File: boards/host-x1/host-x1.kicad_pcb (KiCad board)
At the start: 4 copper layers, 91 x 83 mm, 231 parts, among them J1 CONN_3_PWROUT, J2 XILINX_JTAG, J3 STARSHIPRAIDER_IOBOARD_HOST, J4 BEL_FUSE_0826-1G1T-23-F, J5 PMOD_HEADER, M1 LOGO_LONGTHING, M2 LOGO_ROHS, M3 LOGO_WEEE, M4 HOLE, M5 HOLE, M6 HOLE, M7 HOLE, Q1 SSM6N58NU, Q2 SSM6N58NU, Q3 SSM6N58NU, Q4 SSM6N58NU, SW1 SW_Push, U1 OLK-T_3-W12P-C, U10 DSC6102CI2A-100.0000, U11 S25FS064S_BGA, U2 XC7A100T-1FTG256C, U3 LTC3374-QFN, U4 S27KS0641DPBHI02, U5 S27KS0641DPBHI02, U6 S27KS0641DPBHI02, U7 S27KS0641DPBHI02, U8 KSZ9031RN, U9 DSC6101CI2A-025.0000

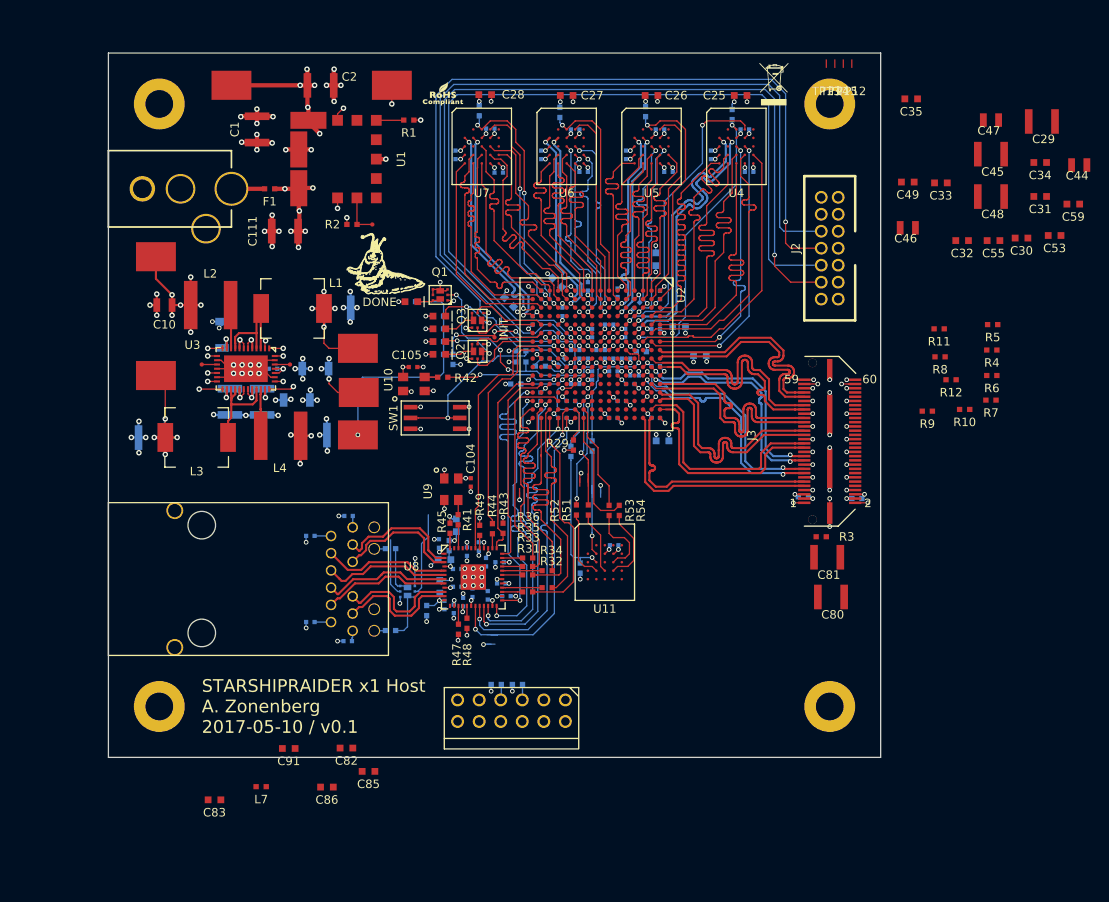
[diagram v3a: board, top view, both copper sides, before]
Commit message: Miscellaneous detail routing. Added some PMOD header connections
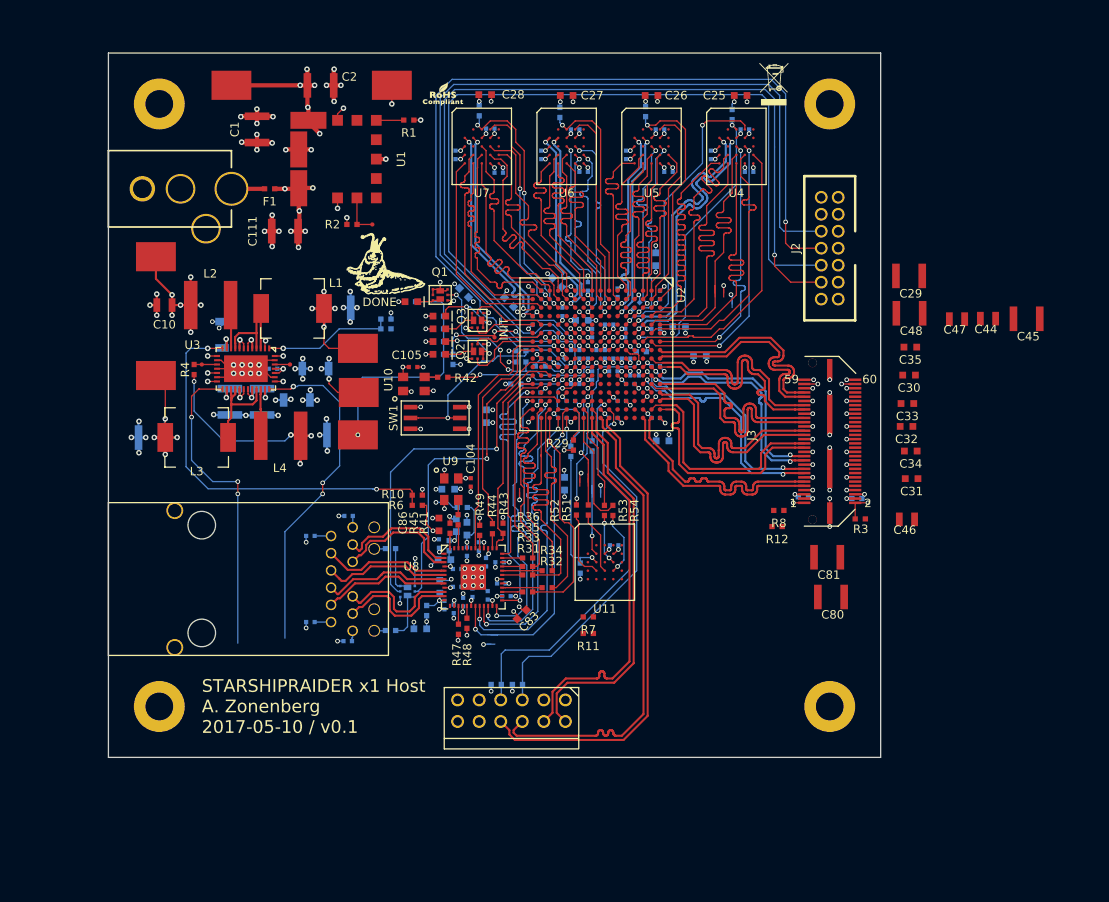
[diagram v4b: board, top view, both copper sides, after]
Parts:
- C49, C53, C55, C59, C82, C85, C91, L7, R5, R9, TP12, TP15: moved to B.Cu
- moved R4 94.0 mm to (39.1, 55.3), turned to 270 degrees
- moved C59 72.6 mm to (70.9, 46.2), turned to 315 degrees
- moved R5 71.5 mm to (61.7, 50.5)
- moved R6 69.4 mm to (65.4, 71.3)
- moved R10 65.3 mm to (65.4, 70.1), turned to 180 degrees
- moved R9 64.7 mm to (61.7, 49.4), turned to 180 degrees
- moved C55 58.1 mm to (82.8, 68.8), turned to 270 degrees
- moved C49 56.8 mm to (73.5, 60.8), turned to 90 degrees
- moved C53 56.6 mm to (84.8, 49.5)
- moved R11 54.8 mm to (85.5, 86.4)
- moved R7 53.9 mm to (85.5, 84.5)
- moved C83 42.3 mm to (77.7, 84.2), turned to 45 degrees
- moved L7 40.5 mm to (70.7, 71.5), turned to 180 degrees
- moved C34 37.3 mm to (123.5, 64.9)
- moved C31 36.5 mm to (123.7, 68.2)
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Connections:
- U2 pad E15: /Line Card/SCOPE_SCL -> Net-(U2-PadE15)
- U2 pad F15: /Line Card/SCOPE_SDA -> Net-(U2-PadF15)
- U2 pad G12: /Line Card/SCOPE_LE_N -> /Line Card/OE5
- U2 pad G15: Net-(U2-PadG15) -> /Line Card/SCOPE_SDA
- U2 pad G16: /Line Card/I2C_SCL -> /Line Card/SCOPEOUT_N
- U2 pad H11: /Line Card/SCOPE_LE_P -> /Line Card/TXD5
- U2 pad H12: /Line Card/SCOPEOUT_P -> /Line Card/OE4
- U2 pad H13: /Line Card/SCOPEOUT_N -> /Line Card/I2C_SCL
- U2 pad H14: Net-(U2-PadH14) -> /Line Card/SCOPE_SCL
- U2 pad H16: /Line Card/OE4 -> /Line Card/SCOPEOUT_P
- U2 pad J15: /Line Card/TXD5 -> /Line Card/SCOPE_LE_P
- U2 pad J16: /Line Card/OE5 -> /Line Card/SCOPE_LE_N
- U2 pad N13: /Flash / Ethernet/ETH_LINK_LED -> Net-(U2-PadN13)
- U2 pad P10: Net-(U2-PadP10) -> /Flash / Ethernet/ETH_LINK_LED
- U2 pad P11: Net-(U2-PadP11) -> /Flash / Ethernet/ETH_ACTIVITY_LED
- U2 pad P13: /Flash / Ethernet/ETH_ACTIVITY_LED -> Net-(U2-PadP13)
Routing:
- net /Line Card/SCOPEOUT_P: track 0.00 -> 56.9 mm
- net /Line Card/SCOPEOUT_N: track 0.00 -> 56.9 mm
- net /Line Card/SCOPE_LE_N: track 0.00 -> 46.2 mm
- net /Line Card/SCOPE_LE_P: track 0.00 -> 46.2 mm
- net /Power Supply/1V2_FB: track 1.75 -> 47.4 mm, vias 1 -> 2
- net /Line Card/SCOPE_SCL: track 1.86 -> 46.9 mm, vias 0 -> 1
- net /Line Card/SCOPE_SDA: track 1.84 -> 44.0 mm, vias 0 -> 1
- net /GND: track 1017.6 -> 1056.1 mm, vias 184 -> 197
- net /Power Supply/3V3_FB: track 2.97 -> 39.8 mm, vias 1 -> 3
- net /Flash / Ethernet/ETH_ACTIVITY_LED: track 6.75 -> 41.7 mm, vias 0 -> 1
- net /Power Supply/1V8_FB: track 2.75 -> 37.1 mm, vias 1 -> 3
- net /Flash / Ethernet/ETH_LINK_LED: track 9.94 -> 39.3 mm, vias 0 -> 1
- net /1V8: track 430.4 -> 459.4 mm, vias 61 -> 66
- net /3V3: track 261.1 -> 280.0 mm, vias 19 -> 20
- net /Power Supply/1V0_FB: track 1.65 -> 15.3 mm
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
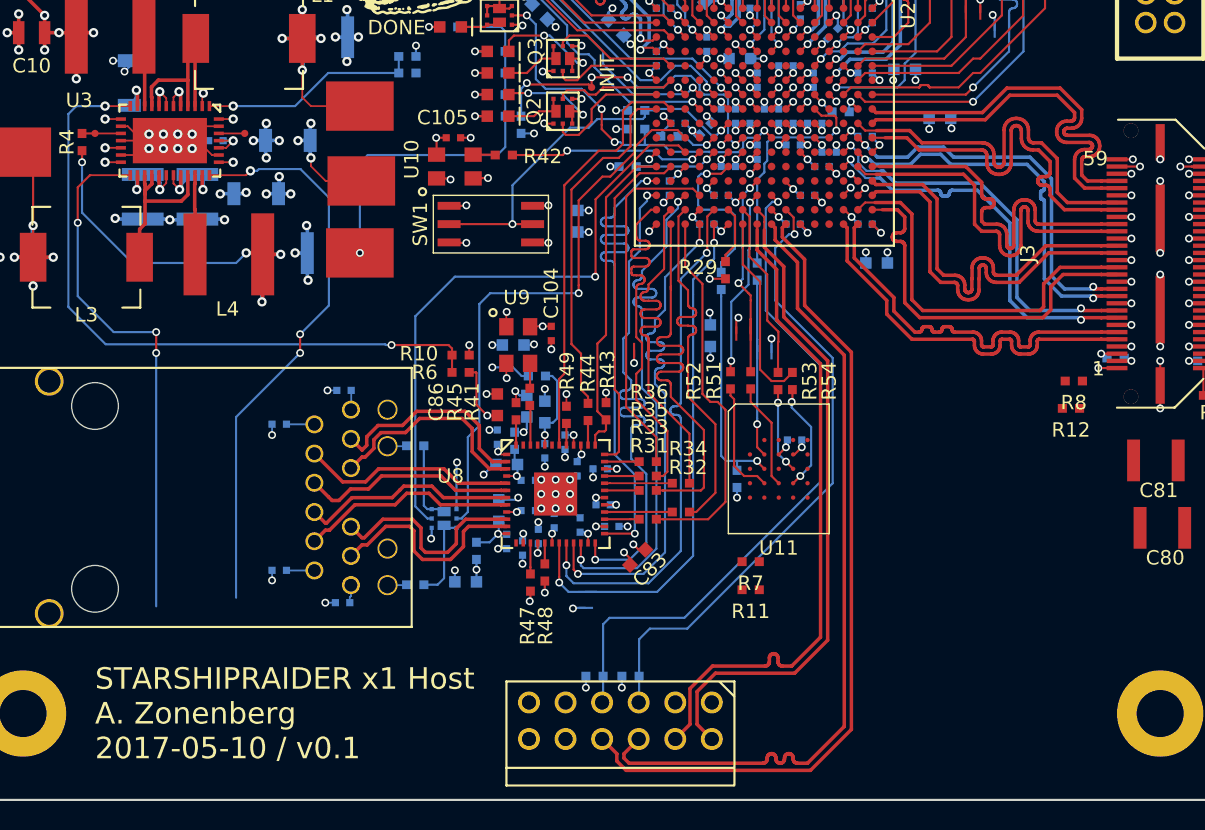
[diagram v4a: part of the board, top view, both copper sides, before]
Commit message: Totally rerouted data lines to I/O header to reduce bottom layer routing congestion
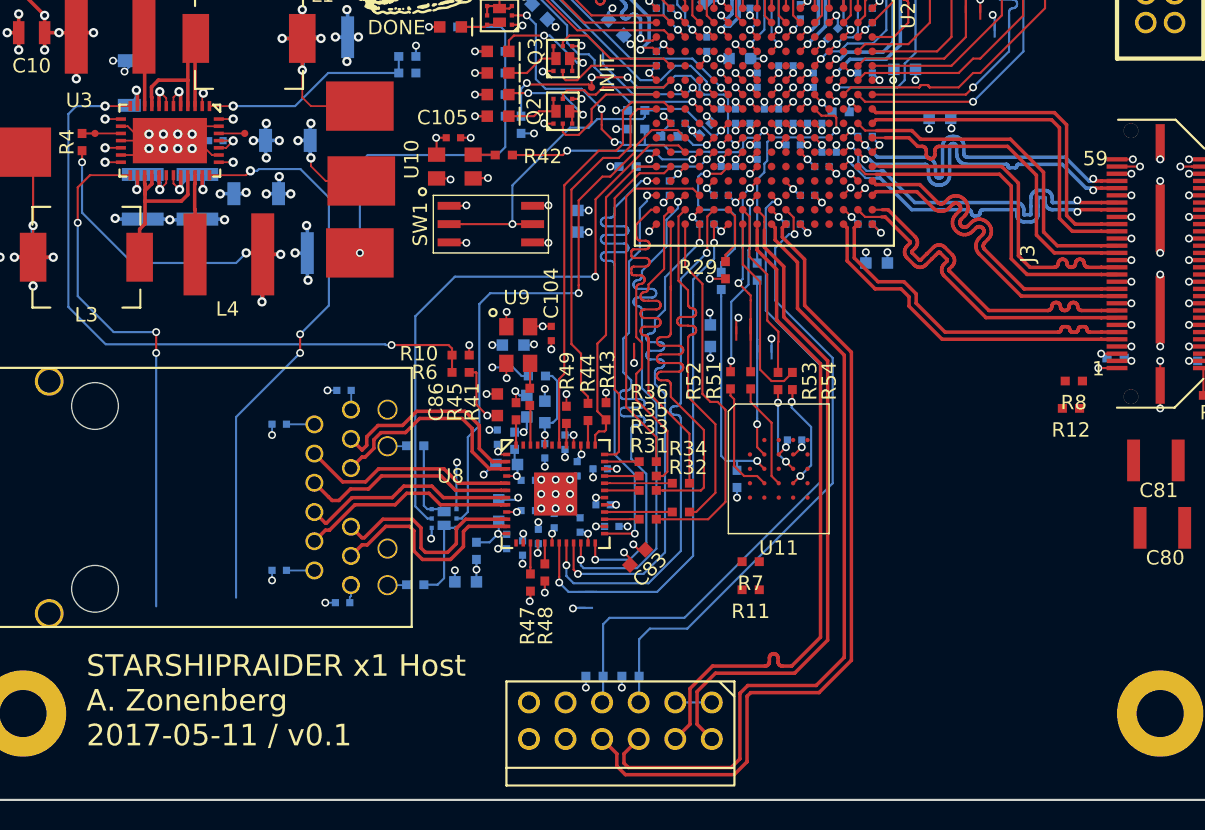
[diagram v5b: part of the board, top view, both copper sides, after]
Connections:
- U2 pad A10: /Line Card/RXD6_P -> /Line Card/RXD4_P
- U2 pad A12: /Line Card/RXD5_N -> /Line Card/RXD3_N
- U2 pad A13: /Line Card/RXD4_N -> /Line Card/RXD2_N
- U2 pad A14: /Line Card/RXD4_P -> /Line Card/RXD2_P
- U2 pad A15: /Line Card/RXD3_P -> /Line Card/RXD1_N
- U2 pad A8: /Line Card/RXD7_N -> /Line Card/RXD5_N
- U2 pad A9: /Line Card/RXD7_P -> /Line Card/RXD5_P
- U2 pad B10: /Line Card/RXD2_N -> /Line Card/RXD7_N
- U2 pad B11: /Line Card/RXD2_P -> /Line Card/RXD7_P
- U2 pad B12: /Line Card/RXD5_P -> /Line Card/RXD3_P
- U2 pad B15: /Line Card/RXD3_N -> /Line Card/RXD1_P
- U2 pad B9: /Line Card/RXD6_N -> /Line Card/RXD4_N
- U2 pad C11: /Line Card/RXD1_N -> /Line Card/RXD6_N
- U2 pad C12: /Line Card/RXD1_P -> /Line Card/RXD6_P
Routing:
- net /Line Card/RXD1_P: track 27.7 -> 24.0 mm, vias 2 -> 0
- net /Line Card/RXD1_N: track 27.6 -> 24.1 mm, vias 2 -> 0
- net /Line Card/RXD2_P: track 27.1 -> 24.0 mm, vias 2 -> 0
- net /Line Card/RXD4_N: track 27.0 -> 24.0 mm
- net /Line Card/RXD4_P: track 27.0 -> 24.0 mm
- net /Line Card/RXD2_N: track 27.0 -> 24.0 mm, vias 2 -> 0
- net /Line Card/RXD0_N: track 27.1 -> 24.1 mm
- net /Line Card/RXD0_P: track 27.0 -> 24.0 mm
- net /Line Card/RXD5_N: track 27.0 -> 24.0 mm
- net /Line Card/RXD5_P: track 27.0 -> 24.0 mm
- net /Line Card/RXD7_N: track 26.9 -> 23.9 mm, vias 0 -> 2
- net /Line Card/RXD6_N: track 27.0 -> 24.0 mm, vias 0 -> 2
- net /Line Card/RXD7_P: track 26.9 -> 24.0 mm, vias 0 -> 2
- net /Line Card/RXD3_P: track 27.0 -> 24.1 mm
- net /Line Card/RXD6_P: track 27.0 -> 24.1 mm, vias 0 -> 2
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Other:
- board text added: "STARSHIPRAIDER x1 Host A. Zonenberg 2017-05-11 / v0.1"
- board text removed: "STARSHIPRAIDER x1 Host A. Zonenberg 2017-05-10 / v0.1"

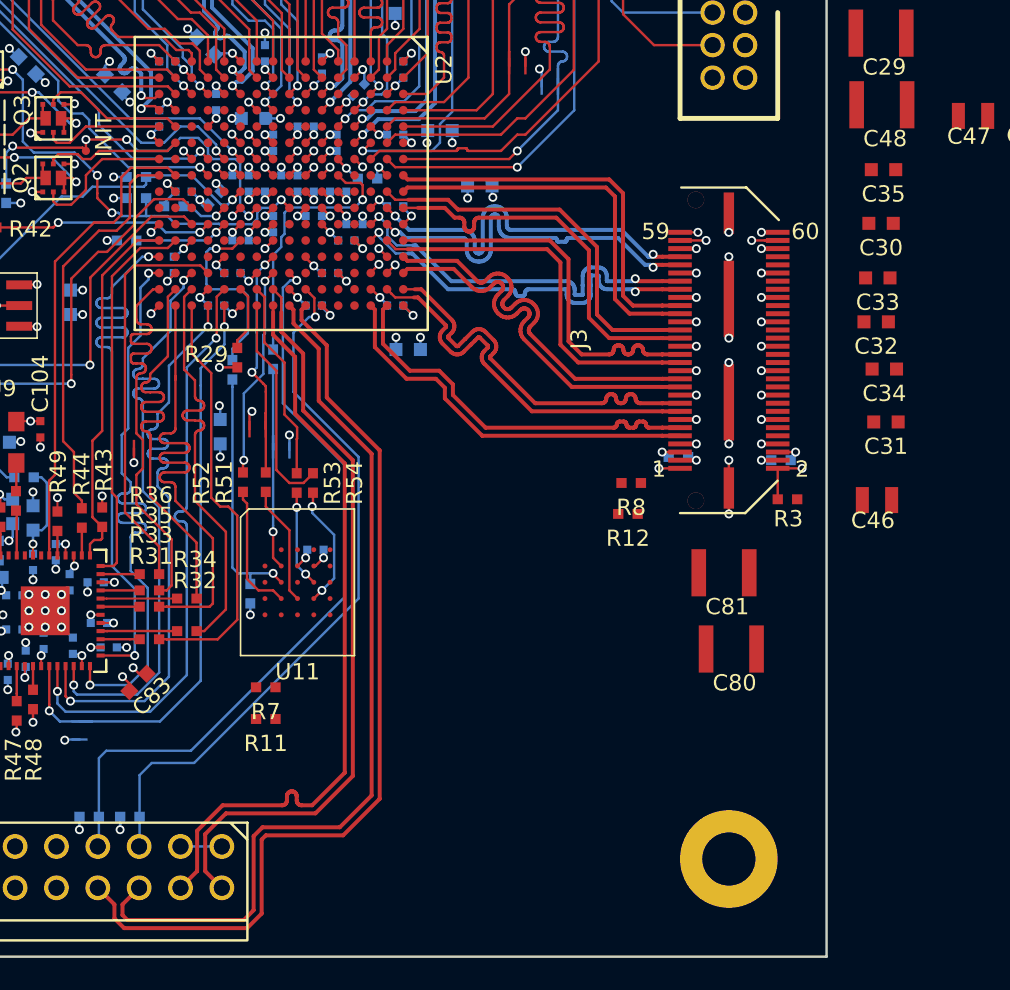
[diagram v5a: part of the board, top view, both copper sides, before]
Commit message: Added PMOD expansion header. Routed out OE/TX lines
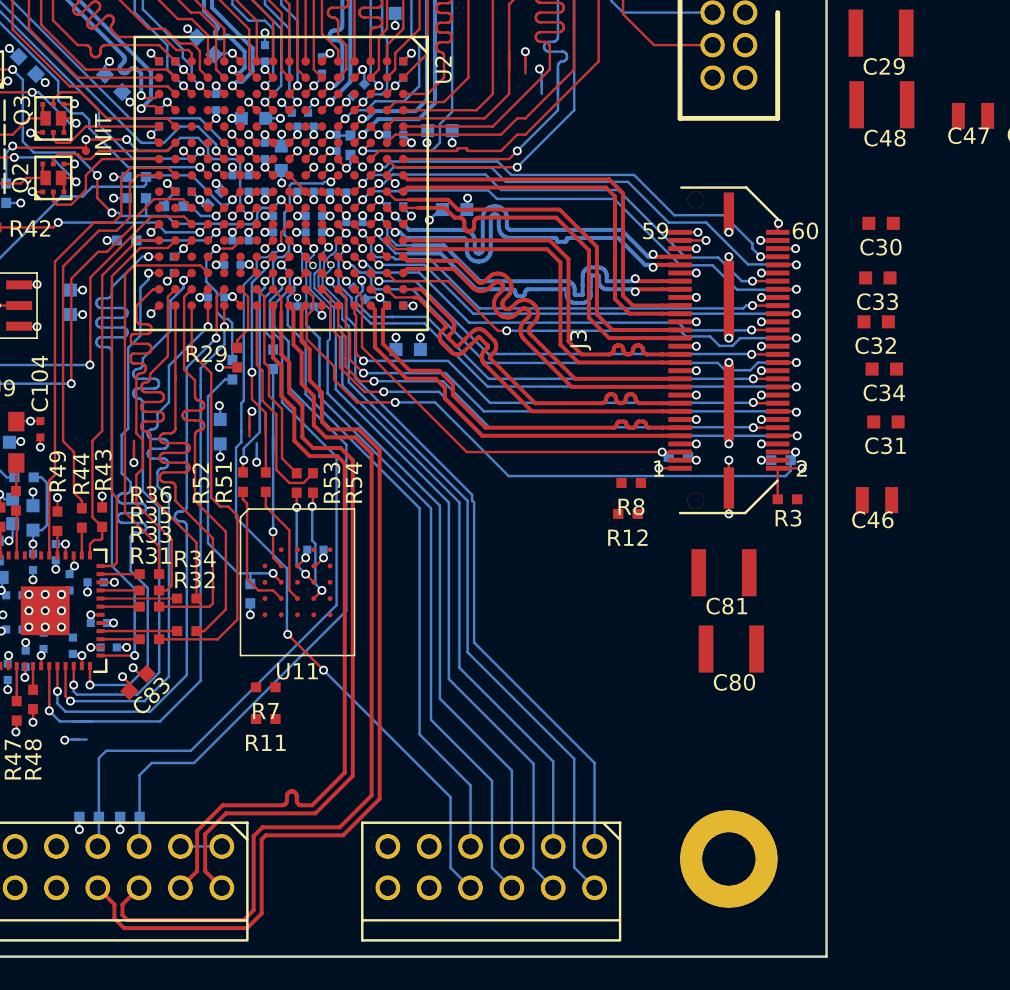
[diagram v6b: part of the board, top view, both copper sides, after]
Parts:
- added J6: PMOD_HEADER, azonenberg_pcb:CONN_HEADER_2.54MM_2x6_RA_PMOD_HOST, F.Cu at (99.4, 95.5)
- C35: moved to B.Cu
- moved C35 37.0 mm to (86.5, 52.0), turned to 90 degrees
- moved C60 3.90 mm to (87.7, 49.1), turned to 180 degrees
- moved R23 2.30 mm to (90.8, 51.1), turned to 90 degrees
- moved C67 2.19 mm to (91.3, 60.2), turned to 315 degrees
- moved C50 2.12 mm to (97.2, 55.1), turned to 180 degrees
- moved C40 2.06 mm to (88.5, 56.5), turned to 180 degrees
- moved TP21 2.00 mm to (84.8, 69.9)
- moved C43 0.71 mm to (85.5, 51.5)
- moved C77 0.50 mm to (88.0, 61.0)
- moved C61 0.50 mm to (82.5, 60.5)
- moved C66 0.50 mm to (83.5, 58.5)
- moved C54 0.12 mm to (91.0, 55.9)
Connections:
- U2 pad B14: /Line Card/OE6 -> /Line Card/TXD4
- U2 pad C13: /Line Card/OE2 -> /Line Card/TXD5
- U2 pad C14: /Line Card/TXD6 -> /Line Card/OE3
- U2 pad C8: Net-(U2-PadC8) -> /Line Card/OE7
- U2 pad C9: Net-(U2-PadC9) -> /Line Card/OE6
- U2 pad D10: Net-(U2-PadD10) -> /Line Card/TXD6
- U2 pad D11: Net-(U2-PadD11) -> /Line Card/OE5
- U2 pad D13: /Line Card/TXD2 -> /Line Card/OE4
- U2 pad D14: /Line Card/TXD3 -> /Line Card/OE2
- U2 pad D15: /Line Card/OE3 -> /Line Card/I2C_SCL
- U2 pad D16: /Line Card/OE0 -> /Line Card/OE1
- U2 pad D9: Net-(U2-PadD9) -> /Line Card/TXD7
- U2 pad E11: Net-(U2-PadE11) -> /Line Card/PMOD_DQ1
- U2 pad E12: /Line Card/TXD7 -> /Line Card/TXD2
- U2 pad E13: /Line Card/OE7 -> /Line Card/TXD3
- U2 pad E15: Net-(U2-PadE15) -> /Line Card/TXD1
- U2 pad E16: /Line Card/TXD0 -> /Line Card/OE0
- U2 pad F12: /Line Card/TXD1 -> /Line Card/PMOD_DQ5
- U2 pad F13: /Line Card/OE1 -> /Line Card/PMOD_DQ4
- U2 pad F14: /Line Card/TXD4 -> /Line Card/PMOD_DQ0
- U2 pad F15: Net-(U2-PadF15) -> /Line Card/TXD0
- U2 pad G12: /Line Card/OE5 -> /Line Card/PMOD_DQ2
- U2 pad G14: /Line Card/I2C_SDA -> /Line Card/PMOD_DQ3
- U2 pad G15: /Line Card/SCOPE_SDA -> /Line Card/I2C_SDA
- U2 pad H11: /Line Card/TXD5 -> /Line Card/PMOD_DQ7
- U2 pad H12: /Line Card/OE4 -> /Line Card/PMOD_DQ6
- U2 pad H13: /Line Card/I2C_SCL -> /Line Card/SCOPE_SDA
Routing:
- net /Line Card/PMOD_DQ7: track 0.00 -> 48.5 mm, vias 0 -> 3
- net /Line Card/PMOD_DQ4: track 0.00 -> 46.9 mm, vias 0 -> 1
- net /Line Card/PMOD_DQ5: track 0.00 -> 46.5 mm, vias 0 -> 1
- net /Line Card/PMOD_DQ1: track 0.00 -> 45.9 mm, vias 0 -> 1
- net /Line Card/PMOD_DQ6: track 0.00 -> 45.8 mm, vias 0 -> 1
- net /Line Card/PMOD_DQ2: track 0.00 -> 43.0 mm, vias 0 -> 1
- net /Line Card/PMOD_DQ0: track 0.00 -> 42.2 mm, vias 0 -> 1
- net /Line Card/PMOD_DQ3: track 0.00 -> 40.3 mm, vias 0 -> 1
- net /Line Card/I2C_SDA: track 1.73 -> 39.6 mm, vias 1 -> 2
- net /Line Card/TXD0: track 0.00 -> 36.3 mm, vias 0 -> 2
- net /Line Card/TXD2: track 0.00 -> 35.2 mm, vias 0 -> 2
- net /Line Card/TXD1: track 0.00 -> 34.6 mm, vias 0 -> 2
- net /Line Card/TXD3: track 0.00 -> 32.6 mm, vias 0 -> 2
- net /Line Card/OE0: track 0.00 -> 32.0 mm, vias 0 -> 2
- net /Line Card/TXD7: track 0.00 -> 31.4 mm, vias 0 -> 2
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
